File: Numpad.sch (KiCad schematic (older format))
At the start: 55 parts, among them J1 USB_B_Mini, SW0 0, SW1 1, SW2 2, SW3 3, SW4 4, SW5 5, SW6 6, SW7 7, SW8 8, SW9 9, U1 ATmega32U4-AU, Y1 16MHz

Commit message: ground planes in, thinking about ordering
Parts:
- D0, D1, D2, D3, D4, D5, D6, D7, D8, D9, DAst1, DDel1, DDiv1, DEnt1, DMns1, DMns2, DNum1, DPls1: footprint Diode_SMD:D_0603_1608Metric_Pad1.05x0.95mm_HandSolder -> Diode_SMD:D_SOD-323_HandSoldering
- J1: footprint AcheronConnectors:USB_MiniB_XM7D-0512 -> digikey-kicad-library:USB_Mini_B_Female_548190519; symbol Connector:USB_B_Mini -> dk_USB-DVI-HDMI-Connectors:0548190519
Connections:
- net Col4: now also U1.19 (PD1); no longer U1.25 (PD4)
- net D+: now also R3.1; no longer R2.1
- net D-: now also R2.1; no longer R3.1
- net Row5: now also U1.26 (PD6); no longer U1.37 (PF6)
- net at J1.2: now also R2.2; no longer R3.2
- net at J1.3: now also R3.2; no longer R2.2
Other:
- moved on the sheet: R2, R3
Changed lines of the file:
@@
 L power:+5V #PWR04
 U 1 1 5D778839
-P 2850 2550
-F 0 "#PWR04" H 2850 2400 50  0001 C CNN
-F 1 "+5V" V 2850 2650 50  0000 L CNN
-F 2 "" H 2850 2550 50  0001 C CNN
-F 3 "" H 2850 2550 50  0001 C CNN
-	1    2850 2550
+P 2700 2700
+F 0 "#PWR04" H 2700 2550 50  0001 C CNN
+F 1 "+5V" V 2600 2700 50  0000 L CNN
+F 2 "" H 2700 2700 50  0001 C CNN
+F 3 "" H 2700 2700 50  0001 C CNN
+	1    2700 2700
 	0    1    1    0
 $EndComp
@@
 L Device:R_Small R2
 U 1 1 5D77A039
-P 3050 2900
-F 0 "R2" V 2854 2900 50  0000 C CNN
-F 1 "22" V 2945 2900 50  0000 C CNN
-F 2 "Resistor_SMD:R_0603_1608Metric_Pad1.05x0.95mm_HandSolder" H 3050 2900 50  0001 C CNN
-F 3 "~" H 3050 2900 50  0001 C CNN
-	1    3050 2900
+P 3000 2800
+F 0 "R2" V 2804 2800 50  0000 C CNN
+F 1 "22" V 2895 2800 50  0000 C CNN
+F 2 "Resistor_SMD:R_0603_1608Metric_Pad1.05x0.95mm_HandSolder" H 3000 2800 50  0001 C CNN
+F 3 "~" H 3000 2800 50  0001 C CNN
+	1    3000 2800
 	0    1    1    0
 $EndComp
@@
 L Device:R_Small R3
 U 1 1 5D77B44C
-P 3050 3000
-F 0 "R3" V 3250 3000 50  0000 C CNN
-F 1 "22" V 3150 3000 50  0000 C CNN
-F 2 "Resistor_SMD:R_0603_1608Metric_Pad1.05x0.95mm_HandSolder" H 3050 3000 50  0001 C CNN
-F 3 "~" H 3050 3000 50  0001 C CNN
-	1    3050 3000
-	0    1    1    0
-$EndComp
-$Comp
-L power:GND #PWR03
-U 1 1 5D77DCB3
-P 2400 3300
-F 0 "#PWR03" H 2400 3050 50  0001 C CNN
-F 1 "GND" V 2405 3127 50  0000 C CNN
-F 2 "" H 2400 3300 50  0001 C CNN
-F 3 "" H 2400 3300 50  0001 C CNN
-	1    2400 3300
-	1    0    0    -1
-$EndComp
-$Comp
-L Connector:USB_B_Mini J1
+P 3000 2900
+F 0 "R3" V 3200 2900 50  0000 C CNN
+F 1 "22" V 3100 2900 50  0000 C CNN
+F 2 "Resistor_SMD:R_0603_1608Metric_Pad1.05x0.95mm_HandSolder" H 3000 2900 50  0001 C CNN
+F 3 "~" H 3000 2900 50  0001 C CNN
+	1    3000 2900
+	0    1    1    0
+$EndComp
+$Comp
+L dk_USB-DVI-HDMI-Connectors:0548190519 J1
 U 1 1 5D776B8C
 P 2400 2900
 F 0 "J1" H 2457 3367 50  0000 C CNN
 F 1 "USB_B_Mini" H 2457 3276 50  0000 C CNN
-F 2 "AcheronConnectors:USB_MiniB_XM7D-0512" H 2550 2850 50  0001 C CNN
+F 2 "digikey-kicad-library:USB_Mini_B_Female_548190519" H 2550 2850 50  0001 C CNN
 F 3 "~" H 2550 2850 50  0001 C CNN
 	1    2400 2900
@@
 F 0 "DNum1" V 7804 1318 50  0000 L CNN
 F 1 "1N4148W" V 7895 1318 50  0000 L CNN
-F 2 "Diode_SMD:D_0603_1608Metric_Pad1.05x0.95mm_HandSolder" V 7850 1250 50  0001 C CNN
+F 2 "Diode_SMD:D_SOD-323_HandSoldering" V 7850 1250 50  0001 C CNN
 F 3 "~" V 7850 1250 50  0001 C CNN
 	1    7850 1250
@@
 F 0 "DDiv1" V 8704 1318 50  0000 L CNN
 F 1 "1N4148W" V 8795 1318 50  0000 L CNN
-F 2 "Diode_SMD:D_0603_1608Metric_Pad1.05x0.95mm_HandSolder" V 8750 1250 50  0001 C CNN
+F 2 "Diode_SMD:D_SOD-323_HandSoldering" V 8750 1250 50  0001 C CNN
 F 3 "~" V 8750 1250 50  0001 C CNN
 	1    8750 1250
@@
 F 0 "DAst1" V 9604 1318 50  0000 L CNN
 F 1 "1N4148W" V 9695 1318 50  0000 L CNN
-F 2 "Diode_SMD:D_0603_1608Metric_Pad1.05x0.95mm_HandSolder" V 9650 1250 50  0001 C CNN
+F 2 "Diode_SMD:D_SOD-323_HandSoldering" V 9650 1250 50  0001 C CNN
 F 3 "~" V 9650 1250 50  0001 C CNN
 	1    9650 1250
@@
 F 0 "D7" V 7804 2368 50  0000 L CNN
 F 1 "1N4148W" V 7895 2368 50  0000 L CNN
-F 2 "Diode_SMD:D_0603_1608Metric_Pad1.05x0.95mm_HandSolder" V 7850 2300 50  0001 C CNN
+F 2 "Diode_SMD:D_SOD-323_HandSoldering" V 7850 2300 50  0001 C CNN
 F 3 "~" V 7850 2300 50  0001 C CNN
 	1    7850 2300
@@
 F 0 "D8" V 8704 2368 50  0000 L CNN
 F 1 "1N4148W" V 8795 2368 50  0000 L CNN
-F 2 "Diode_SMD:D_0603_1608Metric_Pad1.05x0.95mm_HandSolder" V 8750 2300 50  0001 C CNN
+F 2 "Diode_SMD:D_SOD-323_HandSoldering" V 8750 2300 50  0001 C CNN
 F 3 "~" V 8750 2300 50  0001 C CNN
 	1    8750 2300
@@
 F 0 "D9" V 9604 2368 50  0000 L CNN
 F 1 "1N4148W" V 9695 2368 50  0000 L CNN
-F 2 "Diode_SMD:D_0603_1608Metric_Pad1.05x0.95mm_HandSolder" V 9650 2300 50  0001 C CNN
+F 2 "Diode_SMD:D_SOD-323_HandSoldering" V 9650 2300 50  0001 C CNN
 F 3 "~" V 9650 2300 50  0001 C CNN
 	1    9650 2300
@@
 F 0 "D4" V 7804 3368 50  0000 L CNN
 F 1 "1N4148W" V 7895 3368 50  0000 L CNN
-F 2 "Diode_SMD:D_0603_1608Metric_Pad1.05x0.95mm_HandSolder" V 7850 3300 50  0001 C CNN
+F 2 "Diode_SMD:D_SOD-323_HandSoldering" V 7850 3300 50  0001 C CNN
 F 3 "~" V 7850 3300 50  0001 C CNN
 	1    7850 3300
@@
 F 0 "D5" V 8704 3368 50  0000 L CNN
 F 1 "1N4148W" V 8795 3368 50  0000 L CNN
-F 2 "Diode_SMD:D_0603_1608Metric_Pad1.05x0.95mm_HandSolder" V 8750 3300 50  0001 C CNN
+F 2 "Diode_SMD:D_SOD-323_HandSoldering" V 8750 3300 50  0001 C CNN
 F 3 "~" V 8750 3300 50  0001 C CNN
 	1    8750 3300
@@
 F 0 "D6" V 9604 3368 50  0000 L CNN
 F 1 "1N4148W" V 9695 3368 50  0000 L CNN
-F 2 "Diode_SMD:D_0603_1608Metric_Pad1.05x0.95mm_HandSolder" V 9650 3300 50  0001 C CNN
+F 2 "Diode_SMD:D_SOD-323_HandSoldering" V 9650 3300 50  0001 C CNN
 F 3 "~" V 9650 3300 50  0001 C CNN
 	1    9650 3300
@@
 F 0 "D1" V 7804 4368 50  0000 L CNN
 F 1 "1N4148W" V 7895 4368 50  0000 L CNN
-F 2 "Diode_SMD:D_0603_1608Metric_Pad1.05x0.95mm_HandSolder" V 7850 4300 50  0001 C CNN
+F 2 "Diode_SMD:D_SOD-323_HandSoldering" V 7850 4300 50  0001 C CNN
 F 3 "~" V 7850 4300 50  0001 C CNN
 	1    7850 4300
@@
 F 0 "D2" V 8704 4368 50  0000 L CNN
 F 1 "1N4148W" V 8795 4368 50  0000 L CNN
-F 2 "Diode_SMD:D_0603_1608Metric_Pad1.05x0.95mm_HandSolder" V 8750 4300 50  0001 C CNN
+F 2 "Diode_SMD:D_SOD-323_HandSoldering" V 8750 4300 50  0001 C CNN
 F 3 "~" V 8750 4300 50  0001 C CNN
 	1    8750 4300
@@
 F 0 "D3" V 9604 4368 50  0000 L CNN
 F 1 "1N4148W" V 9695 4368 50  0000 L CNN
-F 2 "Diode_SMD:D_0603_1608Metric_Pad1.05x0.95mm_HandSolder" V 9650 4300 50  0001 C CNN
+F 2 "Diode_SMD:D_SOD-323_HandSoldering" V 9650 4300 50  0001 C CNN
 F 3 "~" V 9650 4300 50  0001 C CNN
 	1    9650 4300
@@
 F 0 "DEnt1" V 10504 4868 50  0000 L CNN
 F 1 "1N4148W" V 10595 4868 50  0000 L CNN
-F 2 "Diode_SMD:D_0603_1608Metric_Pad1.05x0.95mm_HandSolder" V 10550 4800 50  0001 C CNN
+F 2 "Diode_SMD:D_SOD-323_HandSoldering" V 10550 4800 50  0001 C CNN
 F 3 "~" V 10550 4800 50  0001 C CNN
 	1    10550 4800
@@
 F 0 "DDel1" V 9604 5368 50  0000 L CNN
 F 1 "1N4148W" V 9695 5368 50  0000 L CNN
-F 2 "Diode_SMD:D_0603_1608Metric_Pad1.05x0.95mm_HandSolder" V 9650 5300 50  0001 C CNN
+F 2 "Diode_SMD:D_SOD-323_HandSoldering" V 9650 5300 50  0001 C CNN
 F 3 "~" V 9650 5300 50  0001 C CNN
 	1    9650 5300
@@
 F 0 "D0" V 8254 5368 50  0000 L CNN
 F 1 "1N4148W" V 8345 5368 50  0000 L CNN
-F 2 "Diode_SMD:D_0603_1608Metric_Pad1.05x0.95mm_HandSolder" V 8300 5300 50  0001 C CNN
+F 2 "Diode_SMD:D_SOD-323_HandSoldering" V 8300 5300 50  0001 C CNN
 F 3 "~" V 8300 5300 50  0001 C CNN
 	1    8300 5300
@@
 Text GLabel 2300 5300 1    50   Output ~ 0
 Row4
-Text GLabel 4100 5300 1    50   Output ~ 0
+Text GLabel 3100 5300 1    50   Output ~ 0
 Row5
 Text GLabel 1800 5300 1    50   Output ~ 0
@@
 Text GLabel 2500 5300 1    50   Output ~ 0
 Col3
-Text GLabel 2900 5300 1    50   Output ~ 0
+Text GLabel 2600 5300 1    50   Output ~ 0
 Col4
 Text GLabel 2300 6500 3    50   Input ~ 0
 D+
-Text GLabel 3250 2900 2    50   Output ~ 0
+Text GLabel 3200 2900 2    50   Output ~ 0
 D+
 Wire Wire Line
-	2700 2900 2950 2900
-Wire Wire Line
-	2700 3000 2950 3000
-Wire Wire Line
-	3150 2900 3250 2900
-Text GLabel 3250 3000 2    50   Output ~ 0
+	3100 2800 3200 2800
+Text GLabel 3200 2800 2    50   Output ~ 0
 D-
 Wire Wire Line
-	3150 3000 3250 3000
+	3100 2900 3200 2900
 Text GLabel 2400 6500 3    50   Input ~ 0
 D-
@@
 F 0 "DMns1" V 10504 1318 50  0000 L CNN
 F 1 "1N4148W" V 10595 1318 50  0000 L CNN
-F 2 "Diode_SMD:D_0603_1608Metric_Pad1.05x0.95mm_HandSolder" V 10550 1250 50  0001 C CNN
+F 2 "Diode_SMD:D_SOD-323_HandSoldering" V 10550 1250 50  0001 C CNN
 F 3 "~" V 10550 1250 50  0001 C CNN
 	1    10550 1250
 	0    1    1    0
 $EndComp
-Wire Wire Line
-	2700 2700 2850 2700
-Wire Wire Line
-	2850 2700 2850 2550
 $Comp
 L Device:C_Small C8
@@
 F 0 "DPls1" V 10504 3368 50  0000 L CNN
 F 1 "1N4148W" V 10595 3368 50  0000 L CNN
-F 2 "Diode_SMD:D_0603_1608Metric_Pad1.05x0.95mm_HandSolder" V 10550 3300 50  0001 C CNN
+F 2 "Diode_SMD:D_SOD-323_HandSoldering" V 10550 3300 50  0001 C CNN
 F 3 "~" V 10550 3300 50  0001 C CNN
 	1    10550 3300
@@
 F 0 "DMns2" V 10504 2368 50  0000 L CNN
 F 1 "1N4148W" V 10595 2368 50  0000 L CNN
-F 2 "Diode_SMD:D_0603_1608Metric_Pad1.05x0.95mm_HandSolder" V 10550 2300 50  0001 C CNN
+F 2 "Diode_SMD:D_SOD-323_HandSoldering" V 10550 2300 50  0001 C CNN
 F 3 "~" V 10550 2300 50  0001 C CNN
 	1    10550 2300
@@
 Connection ~ 4650 1050
 Connection ~ 4650 1600
+Wire Wire Line
+	2700 2800 2900 2800
+Wire Wire Line
+	2700 2900 2900 2900
+$Comp
+L power:GND #PWR03
+U 1 1 5D77DCB3
+P 2700 3100
+F 0 "#PWR03" H 2700 2850 50  0001 C CNN
+F 1 "GND" V 2600 3050 50  0000 C CNN
+F 2 "" H 2700 3100 50  0001 C CNN
+F 3 "" H 2700 3100 50  0001 C CNN
+	1    2700 3100
+	0    -1   -1   0
+$EndComp
 $EndSCHEMATC

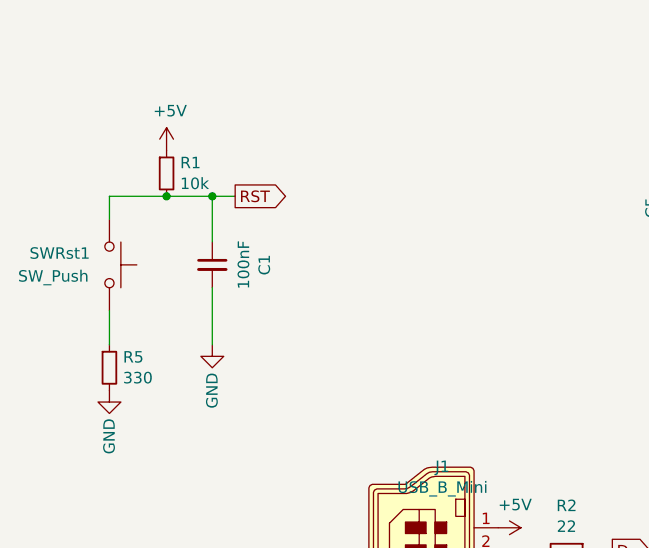
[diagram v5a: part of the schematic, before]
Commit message: two of the capacitors needed larger footprints, have added BoM
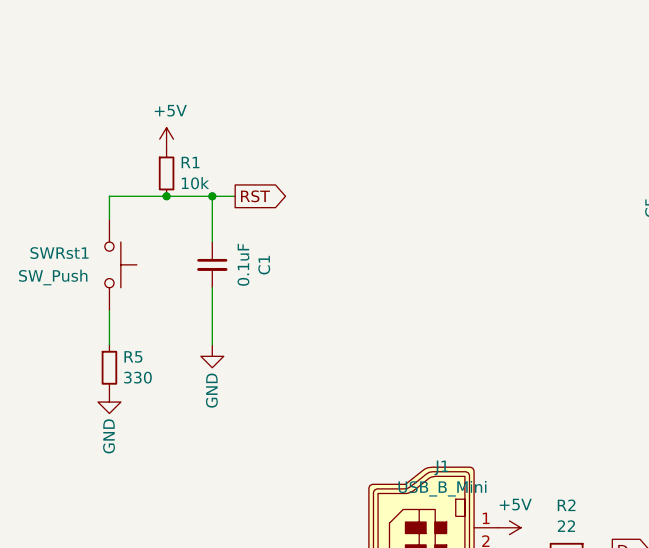
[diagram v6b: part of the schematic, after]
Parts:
- C1: value 100nF -> 0.1uF
- C4, C5: footprint Capacitor_SMD:C_0603_1608Metric_Pad1.05x0.95mm_HandSolder -> Capacitor_SMD:C_0805_2012Metric_Pad1.15x1.40mm_HandSolder
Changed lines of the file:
@@
 F 0 "C4" V 2800 6700 50  0000 C CNN
 F 1 "1uF" V 2700 6700 50  0000 C CNN
-F 2 "Capacitor_SMD:C_0603_1608Metric_Pad1.05x0.95mm_HandSolder" H 2600 6700 50  0001 C CNN
+F 2 "Capacitor_SMD:C_0805_2012Metric_Pad1.15x1.40mm_HandSolder" H 2600 6700 50  0001 C CNN
 F 3 "~" H 2600 6700 50  0001 C CNN
 	1    2600 6700
@@
 P 1450 1550
 F 0 "C1" V 1679 1550 50  0000 C CNN
-F 1 "100nF" V 1588 1550 50  0000 C CNN
+F 1 "0.1uF" V 1588 1550 50  0000 C CNN
 F 2 "Capacitor_SMD:C_0603_1608Metric_Pad1.05x0.95mm_HandSolder" H 1450 1550 50  0001 C CNN
 F 3 "~" H 1450 1550 50  0001 C CNN
@@
 F 0 "C5" V 3829 1300 50  0000 C CNN
 F 1 "4.7uF" V 3738 1300 50  0000 C CNN
-F 2 "Capacitor_SMD:C_0603_1608Metric_Pad1.05x0.95mm_HandSolder" H 3600 1300 50  0001 C CNN
+F 2 "Capacitor_SMD:C_0805_2012Metric_Pad1.15x1.40mm_HandSolder" H 3600 1300 50  0001 C CNN
 F 3 "~" H 3600 1300 50  0001 C CNN
 	1    3600 1300

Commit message: Rotated Pls & Rtn switches, they are loose in the plate in original orientation
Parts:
- C4: footprint Capacitor_SMD:C_0805_2012Metric_Pad1.15x1.40mm_HandSolder -> Capacitor_SMD:C_0603_1608Metric_Pad1.05x0.95mm_HandSolder
- SWEnt1, SWPls1: footprint AcheronMX:MX200VR -> AcheronMX:MX200
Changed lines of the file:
@@
 F 0 "C4" V 2800 6700 50  0000 C CNN
 F 1 "1uF" V 2700 6700 50  0000 C CNN
-F 2 "Capacitor_SMD:C_0805_2012Metric_Pad1.15x1.40mm_HandSolder" H 2600 6700 50  0001 C CNN
+F 2 "Capacitor_SMD:C_0603_1608Metric_Pad1.05x0.95mm_HandSolder" H 2600 6700 50  0001 C CNN
 F 3 "~" H 2600 6700 50  0001 C CNN
 	1    2600 6700
@@
 F 0 "SWEnt1" H 10400 5350 50  0000 L CNN
 F 1 "Ent" H 10400 5150 118 0000 L CNN
-F 2 "AcheronMX:MX200VR" H 10550 5250 50  0001 C CNN
+F 2 "AcheronMX:MX200" H 10550 5250 50  0001 C CNN
 F 3 "" H 10550 5250 50  0001 C CNN
 	1    10550 5250
@@
 F 0 "SWPls1" H 11050 3950 50  0000 L CNN
 F 1 "+" H 10900 3950 118 0000 L CNN
-F 2 "AcheronMX:MX200VR" H 10600 3800 50  0001 C CNN
+F 2 "AcheronMX:MX200" H 10600 3800 50  0001 C CNN
 F 3 "" H 10600 3800 50  0001 C CNN
 	1    10600 3800

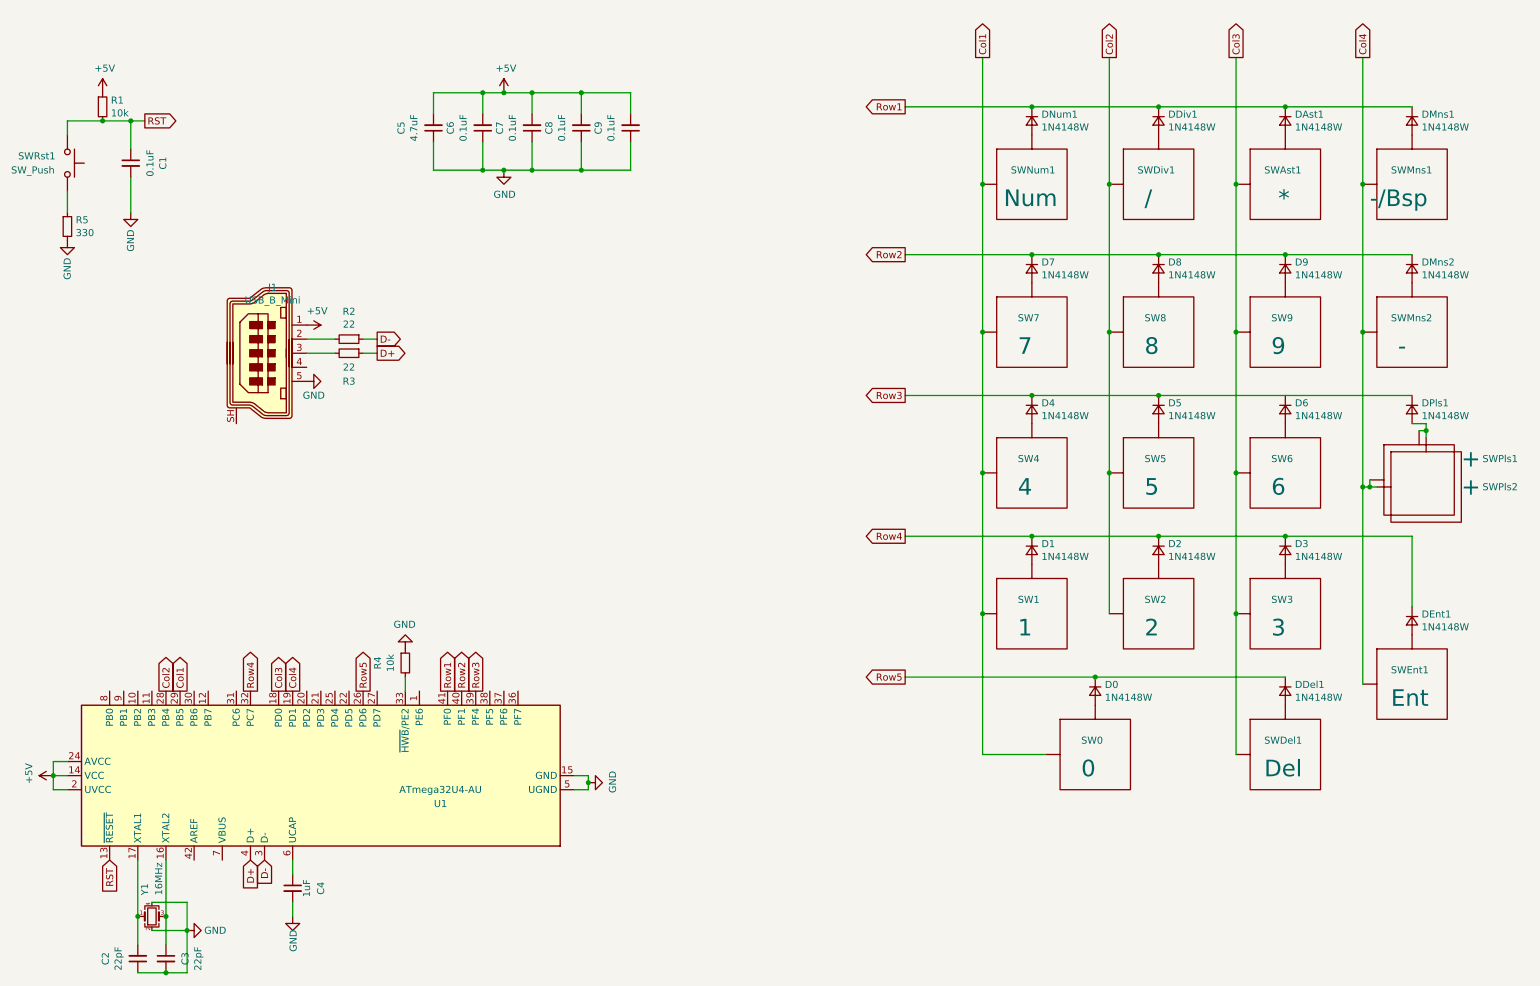
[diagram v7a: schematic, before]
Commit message: I hadnt connected the VBUS, changed it back to 17 keys no option for split plus.
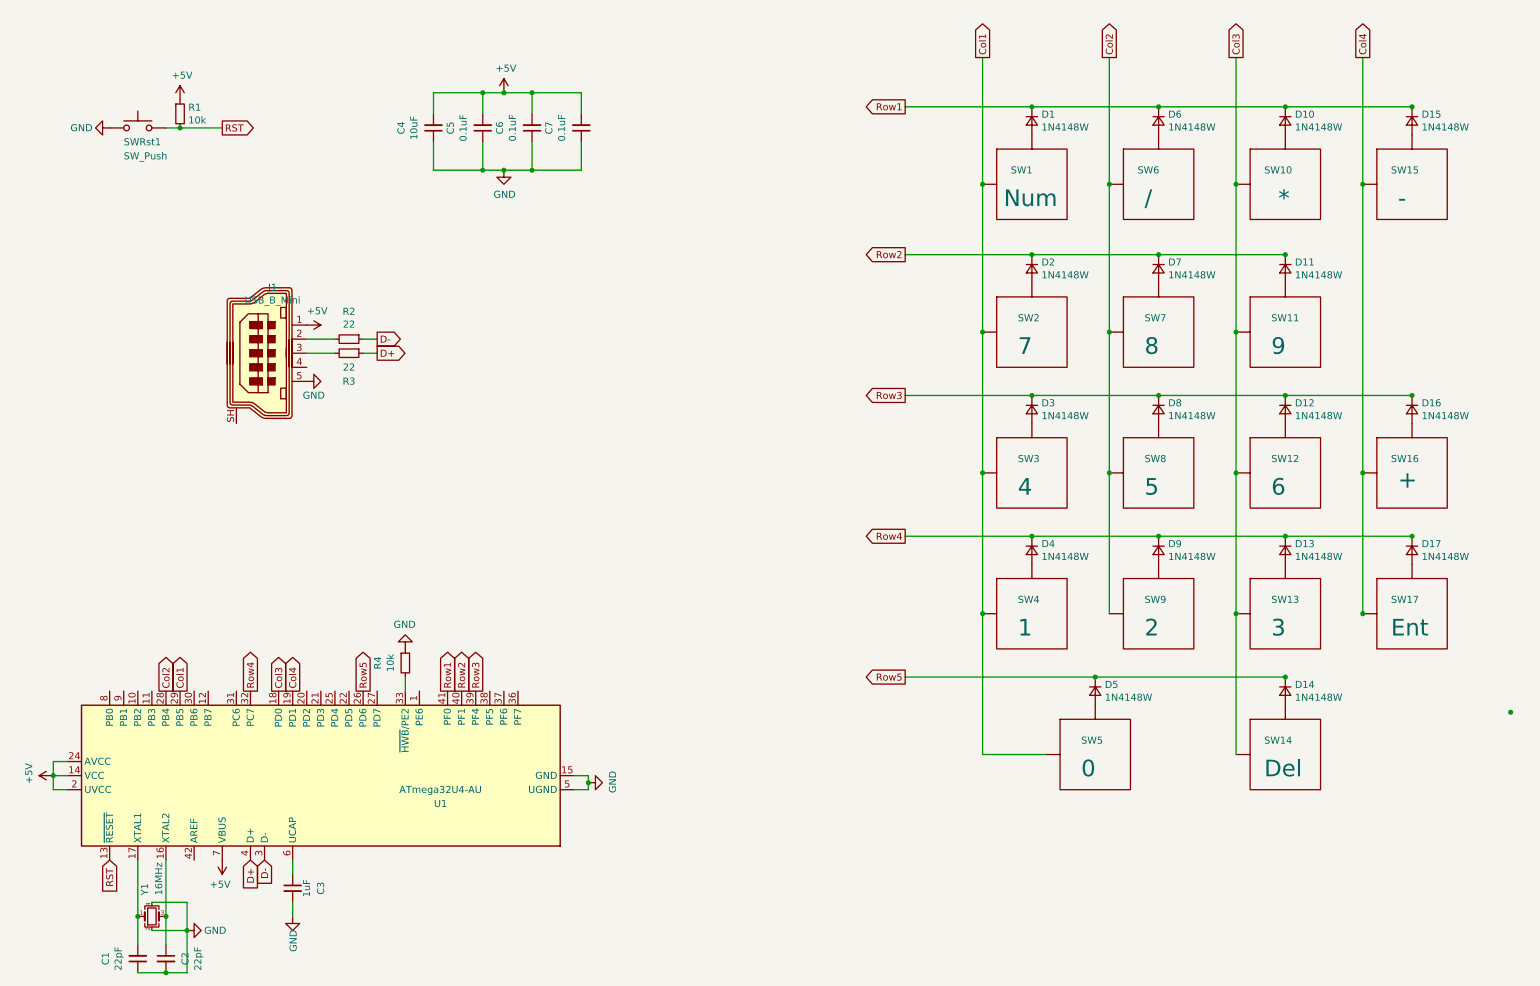
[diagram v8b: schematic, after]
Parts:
- removed C1, C9: 0.1uF, Capacitor_SMD:C_0603_1608Metric_Pad1.05x0.95mm_HandSolder, symbol Device:C_Small
- removed DMns2: 1N4148W, Diode_SMD:D_SOD-323_HandSoldering, symbol Device:D_Small
- removed R5: 330, Resistor_SMD:R_0603_1608Metric_Pad1.05x0.95mm_HandSolder, symbol Device:R_Small
- removed SWMns2: -, AcheronMX:MX100, symbol Acheron:MXSwitch
- removed SWPls2: +, AcheronMX:MX100, symbol Acheron:MXSwitch
- C4: renamed from C5; value 4.7uF -> 10uF
- SW15: renamed from SWMns1; value -/Bsp -> -
- renumbered C2 to C1, C3 to C2, C4 to C3, C6 to C5, C7 to C6, C8 to C7, DNum1 to D1, DAst1 to D10, D9 to D11, D6 to D12, D3 to D13, DDel1 to D14, DMns1 to D15, DPls1 to D16, DEnt1 to D17, D7 to D2, D4 to D3, D1 to D4, D0 to D5, DDiv1 to D6, D8 to D7, D5 to D8, D2 to D9, SWNum1 to SW1, SWAst1 to SW10, SW9 to SW11, SW6 to SW12, SW3 to SW13, SWDel1 to SW14, SWPls1 to SW16, SWEnt1 to SW17, SW7 to SW2, SW4 to SW3, SW1 to SW4, SW0 to SW5, SWDiv1 to SW6, SW8 to SW7, SW5 to SW8, SW2 to SW9
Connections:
- net +5V: now also U1.7 (VBUS)
- net GND: now also SWRst1.1
- net RST: now also SWRst1.2; no longer SWRst1.1
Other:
- moved on the sheet: D17, R1, SW16, SW17, SWRst1
